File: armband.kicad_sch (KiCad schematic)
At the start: 33 parts, among them IC1 STM32MP157AAB3, IC7 S40FC004C1B2C00000, IC9 NXS0506UPZ, J3 MEM2075-00-140-01-A, J4 Conn_01x03, SW1 SW_MEC_5G, SW2 SW_MEC_5G

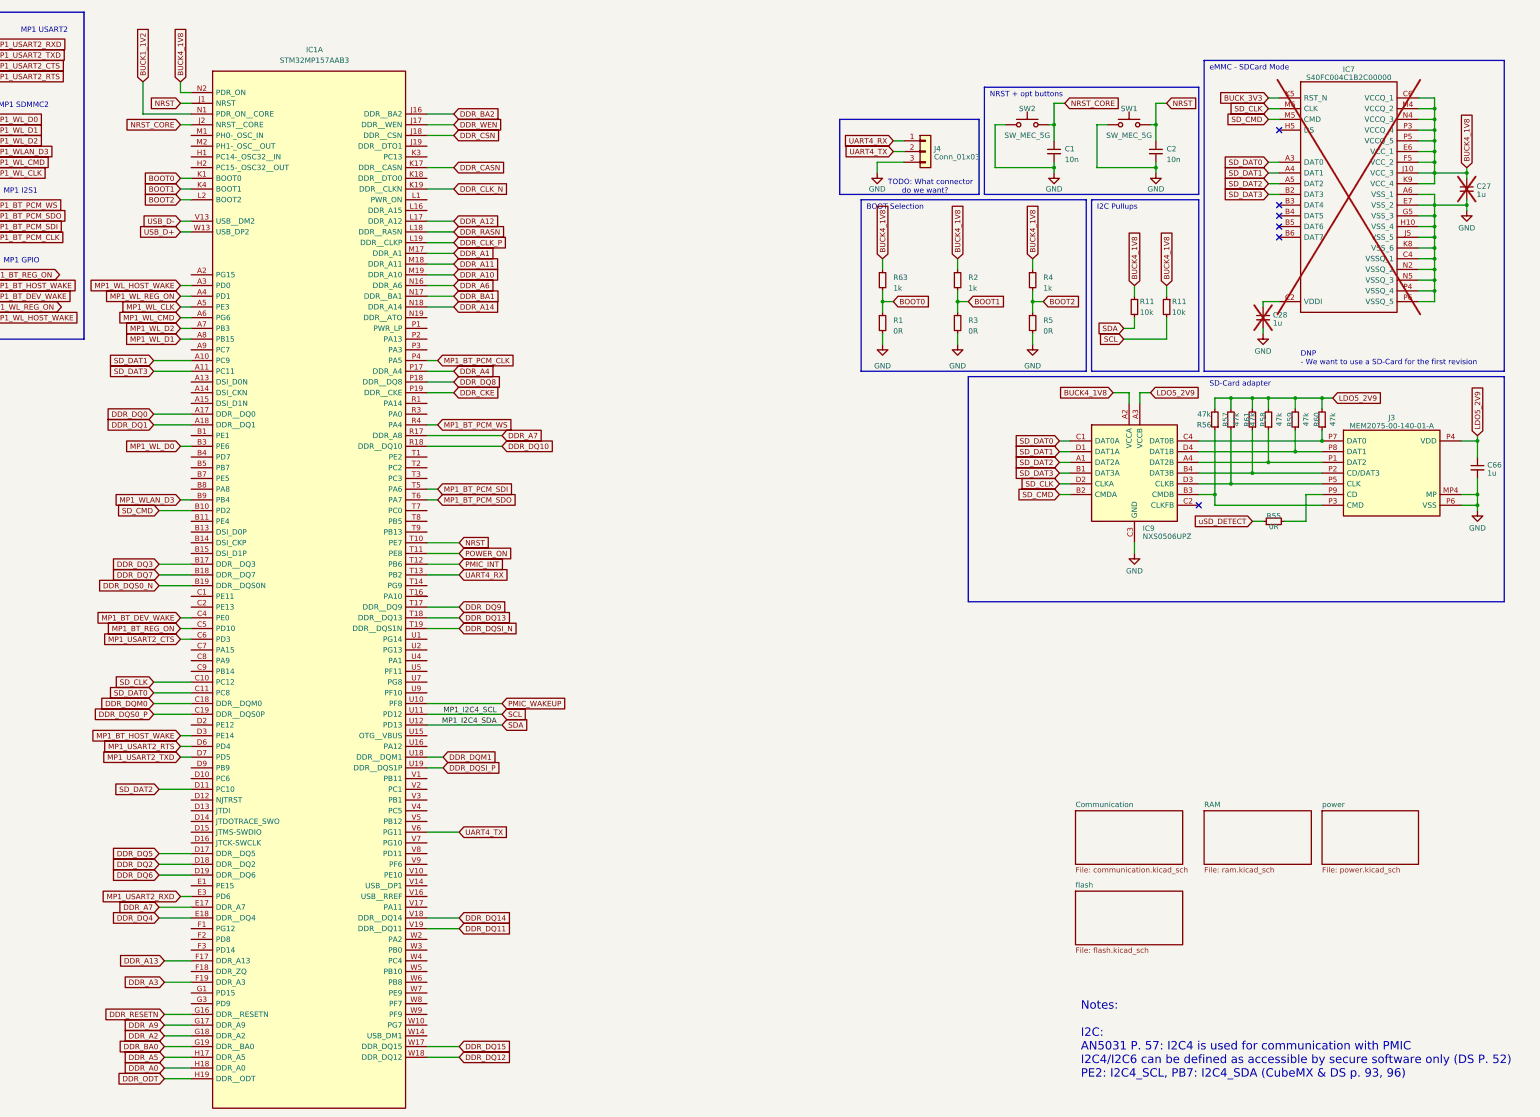
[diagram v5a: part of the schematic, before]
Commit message: removed unneccessary parts + first ram layout iteration
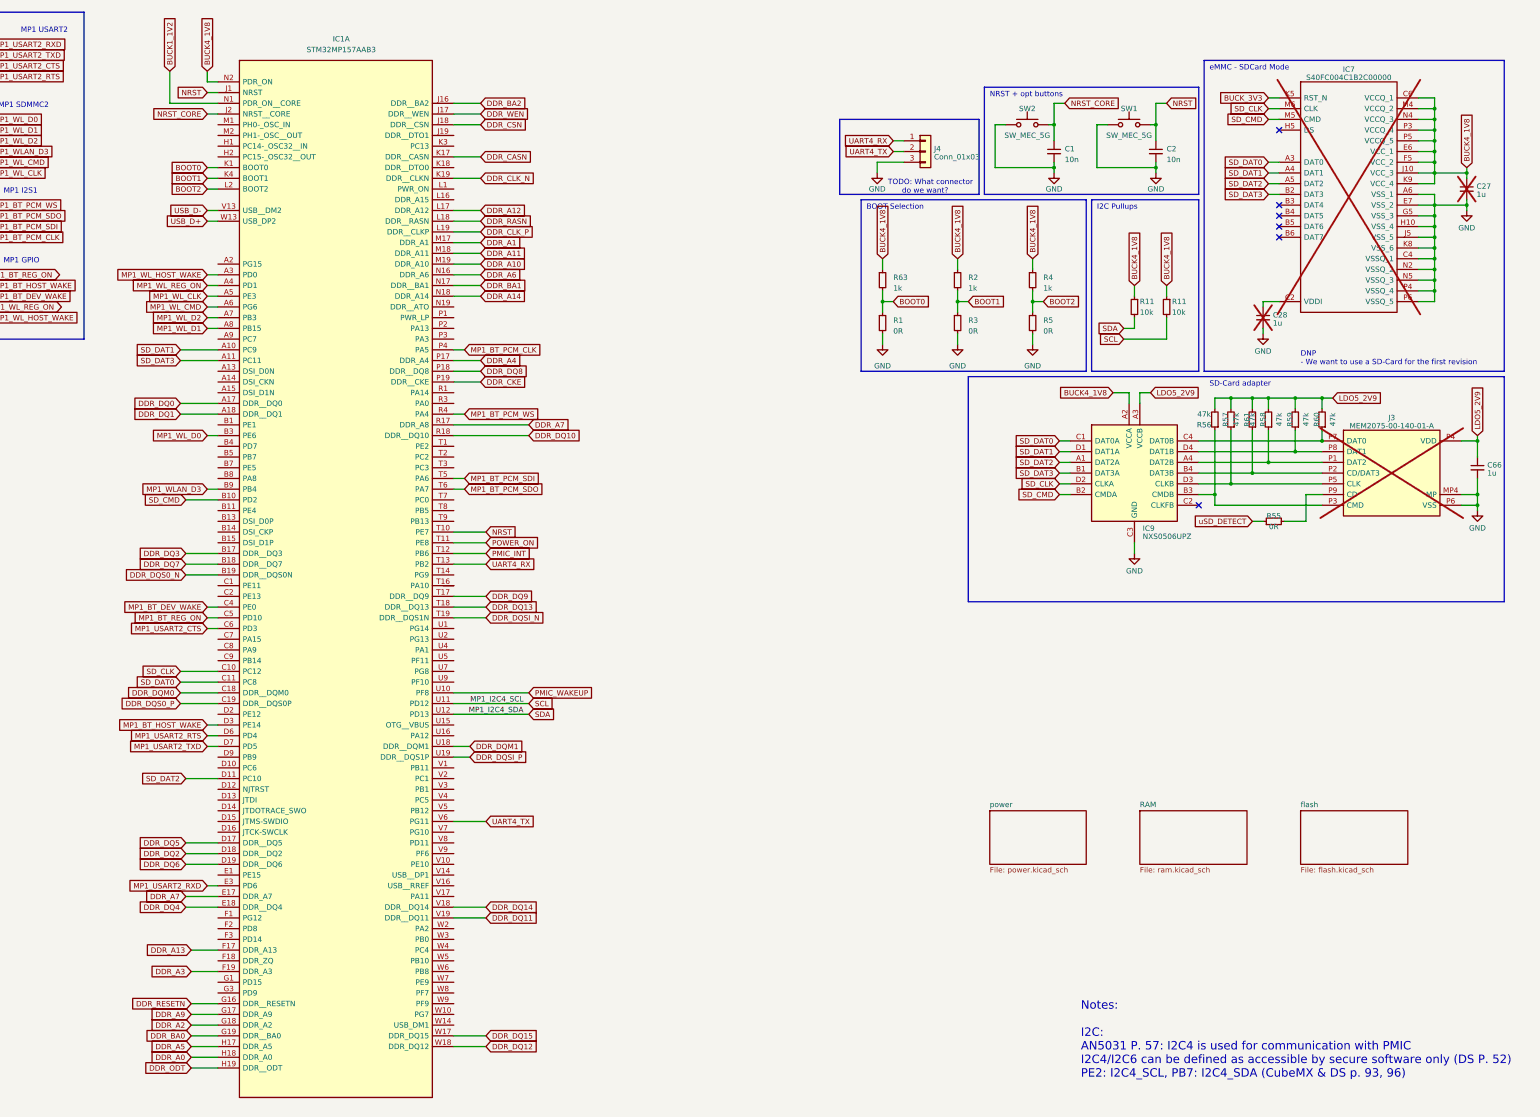
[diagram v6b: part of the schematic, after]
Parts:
- J3: now not fitted
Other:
- removed sheet Communication
- moved on the sheet: IC1A

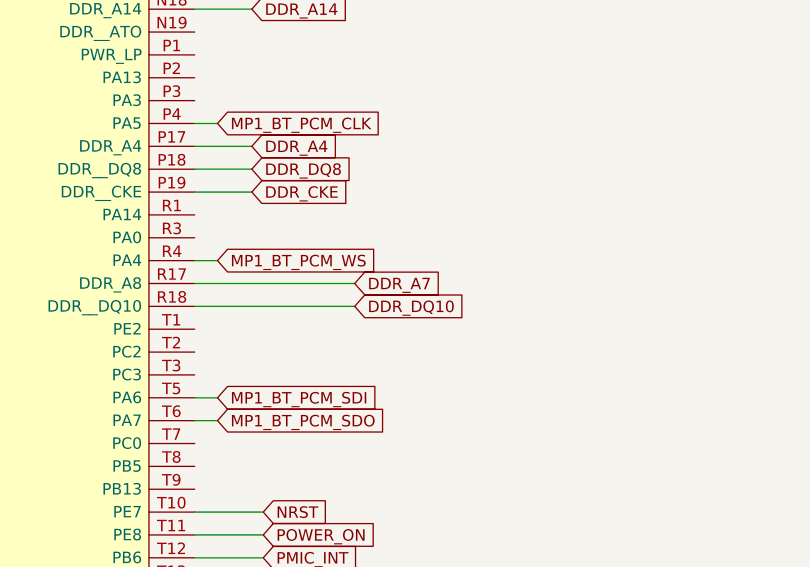
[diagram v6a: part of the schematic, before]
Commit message: Add vias and routes for addr lines
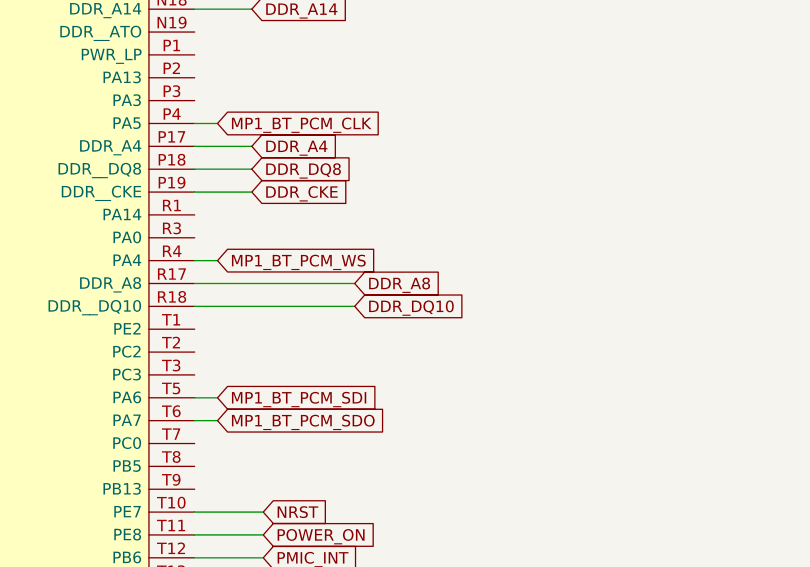
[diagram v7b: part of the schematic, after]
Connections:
- net DDR_A7: no longer IC1.R17 (DDR_A8)
- new net DDR_A8: IC1.R17 (DDR_A8)
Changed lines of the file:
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@@
     )
   )
-  (global_label "DDR_A7" (shape input) (at 170.18 111.76 0) (fields_autoplaced)
+  (global_label "DDR_A8" (shape input) (at 170.18 111.76 0) (fields_autoplaced)
     (effects (font (size 1.27 1.27)) (justify left))
-    (property "Intersheetrefs" "${INTERSHEET_REFS}" (at 180.1615 111.76 0)
+    (property "Intersheetrefs" "${INTERSHEET_REFS}" (at 180.2409 111.76 0)
       (effects (font (size 1.27 1.27)) (justify left) hide)
     )

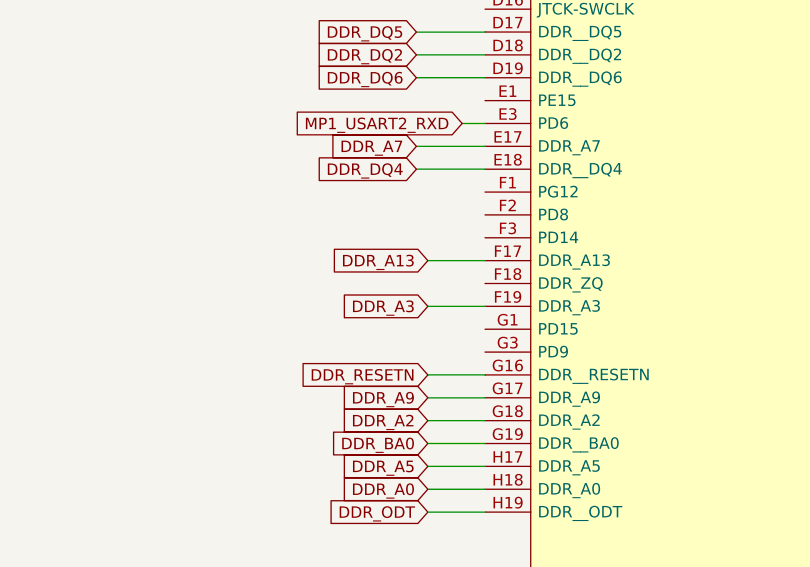
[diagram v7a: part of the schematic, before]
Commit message: connected address pins of ddr3
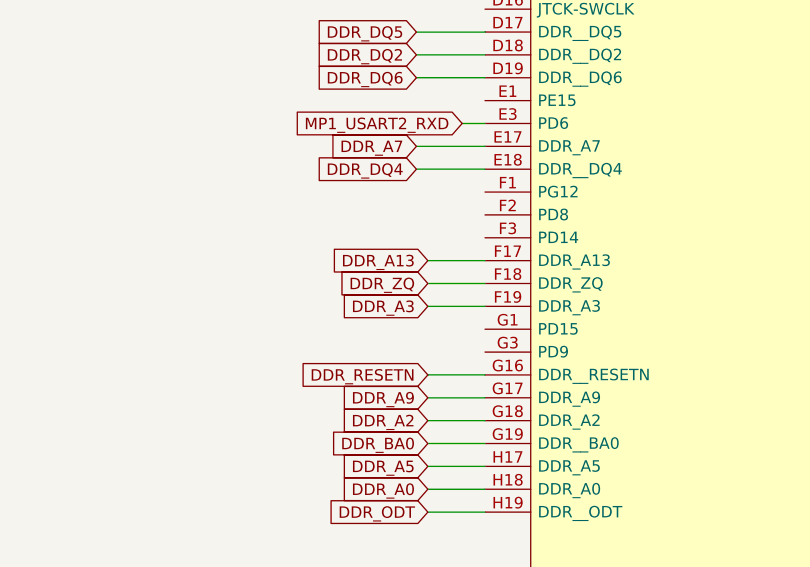
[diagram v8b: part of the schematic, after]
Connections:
- net DDR_ZQ: now reaches IC1.F18 (DDR_ZQ)
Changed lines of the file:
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@@
+    (stroke (width 0) (type default))
+  )
+  (wire (pts (xy 90.17 238.76) (xy 96.52 238.76))
     (stroke (width 0) (type default))
   )
@@
       (effects (font (size 1.27 1.27)) hide)
     )
+  )
+  (global_label "DDR_ZQ" (shape input) (at 90.17 238.76 180) (fields_autoplaced)
+    (effects (font (size 1.27 1.27)) (justify right))
+    (property "Intersheetrefs" "${INTERSHEET_REFS}" (at 45.72 172.72 0)
+      (effects (font (size 1.27 1.27)) hide)
+    )
